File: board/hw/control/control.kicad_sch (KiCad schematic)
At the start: 43 parts, among them IC1 TINY2313, J1 stepper #1, J2 stepper #2, J3 buttons, J4 power, J6 AVR-ISP-10, Q1 MMFTP84W, Q3 2N7002, U1 ULN2003A, U2 ULN2003A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

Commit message: page size adjusted to schematics requirements
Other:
- moved on the sheet: C2, C4, C5, C6, D1, D2, D3, D4, D5, D6, D7, D8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

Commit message: C2 and C4 are not 1206 as they should
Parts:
- C2: footprint Capacitor_SMD:C_0805_2012Metric -> Capacitor_SMD:C_1206_3216Metric_Pad1.33x1.80mm_HandSolder
- C4: footprint Capacitor_SMD:C_0805_2012Metric_Pad1.18x1.45mm_HandSolder -> Capacitor_SMD:C_1206_3216Metric_Pad1.33x1.80mm_HandSolder
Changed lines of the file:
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@@
       (effects (font (size 1.778 1.5113)) (justify left bottom))
     )
-    (property "Footprint" "Capacitor_SMD:C_0805_2012Metric_Pad1.18x1.45mm_HandSolder" (at 116.84 110.49 0)
+    (property "Footprint" "Capacitor_SMD:C_1206_3216Metric_Pad1.33x1.80mm_HandSolder" (at 116.84 110.49 0)
       (effects (font (size 1.27 1.27)) hide)
     )
@@
       (effects (font (size 1.778 1.5113)) (justify left bottom))
     )
-    (property "Footprint" "Capacitor_SMD:C_0805_2012Metric" (at 144.78 72.39 0)
-      (effects (font (size 1.27 1.27)) hide)
-    )
+    (property "Footprint" "Capacitor_SMD:C_1206_3216Metric_Pad1.33x1.80mm_HandSolder" (at 144.78 72.39 0)
+      (effects (font (size 1.27 1.27)) hide)
+    )

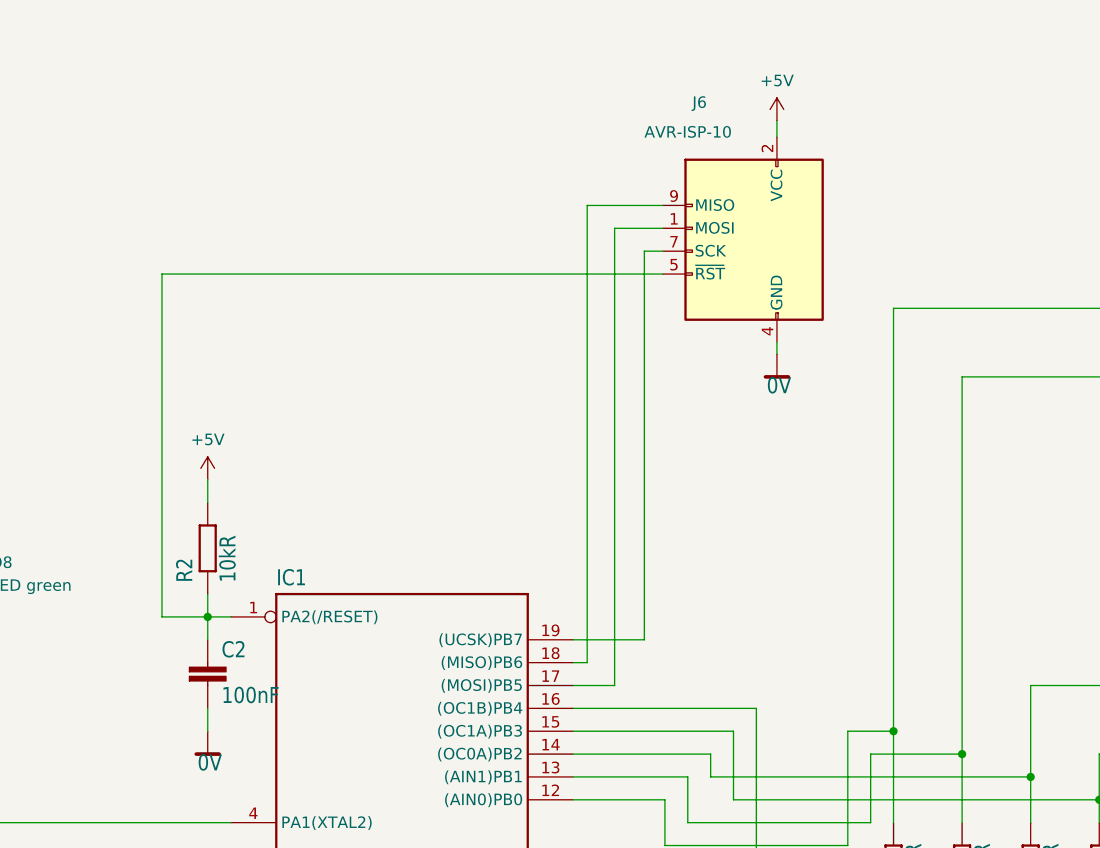
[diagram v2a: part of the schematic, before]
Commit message: added diade so that AVR's ISP can optionaly power the board, but board power will not damage the programmer
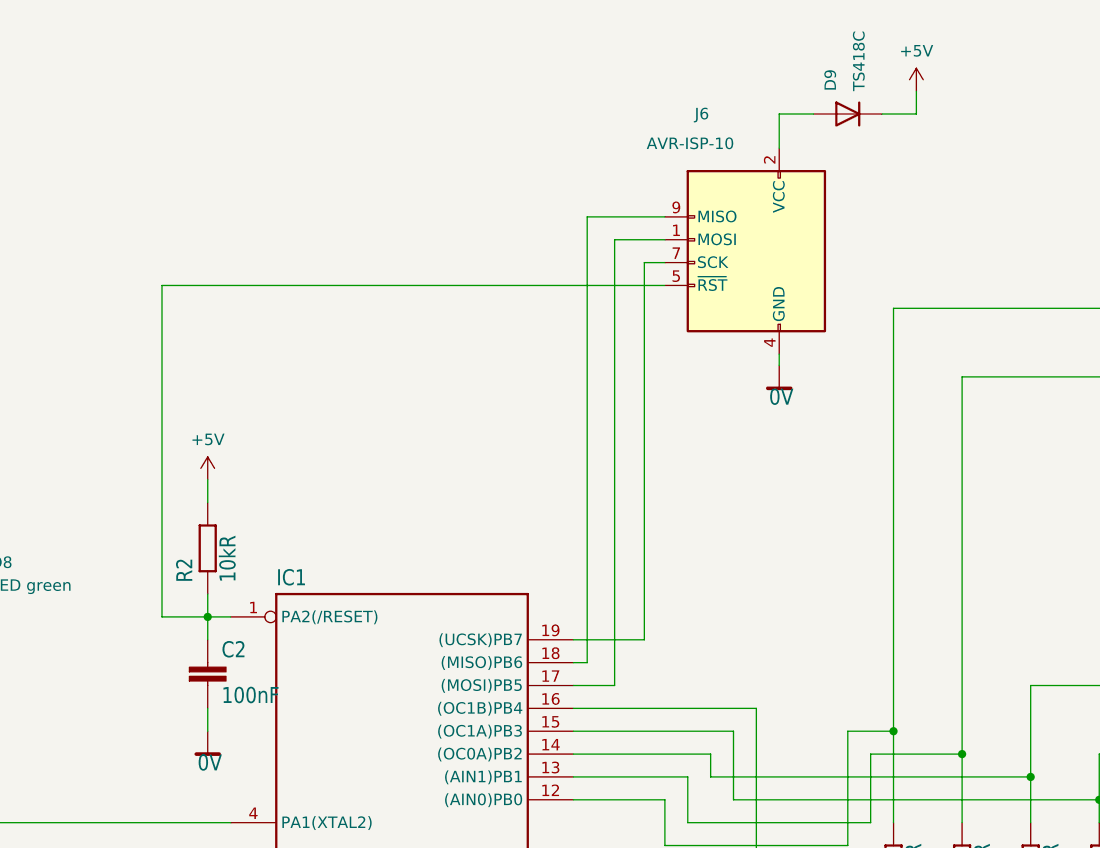
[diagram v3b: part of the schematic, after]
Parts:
- added D9: TS418C, Diode_SMD:D_0805_2012Metric, symbol Diode:CD4148W
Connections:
- net +5V: now also D9.1 (K); no longer J6.2 (VCC)
- new net: D9.2 (A), J6.2 (VCC)
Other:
- moved on the sheet: J6
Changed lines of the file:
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@@
+    (stroke (width 0) (type default))
+  )
+  (wire (pts (xy 223.52 11.43) (xy 223.52 8.89))
     (stroke (width 0) (type default))
   )
@@
     (stroke (width 0) (type default))
   )
+  (wire (pts (xy 208.28 11.43) (xy 212.09 11.43))
+    (stroke (width 0) (type default))
+  )
   (wire (pts (xy 318.135 53.975) (xy 313.69 53.975))
     (stroke (width 0) (type default))
@@
     (stroke (width 0) (type default))
   )
-  (wire (pts (xy 193.294 26.67) (xy 193.294 69.85))
+  (wire (pts (xy 193.294 27.94) (xy 193.294 69.85))
     (stroke (width 0) (type default))
   )
@@
     (stroke (width 0) (type default))
   )
-  (wire (pts (xy 208.026 12.192) (xy 208.026 13.97))
-    (stroke (width 0) (type default))
-  )
   (wire (pts (xy 298.45 135.89) (xy 303.53 135.89))
     (stroke (width 0) (type default))
@@
     (stroke (width 0) (type default))
   )
-  (wire (pts (xy 195.326 21.59) (xy 186.944 21.59))
+  (wire (pts (xy 195.58 22.86) (xy 186.944 22.86))
     (stroke (width 0) (type default))
   )
@@
     (stroke (width 0) (type default))
   )
-  (wire (pts (xy 139.7 29.21) (xy 139.7 67.31))
+  (wire (pts (xy 139.7 30.48) (xy 139.7 67.31))
     (stroke (width 0) (type default))
   )
@@
     (stroke (width 0) (type default))
   )
+  (wire (pts (xy 208.28 39.37) (xy 208.28 38.1))
+    (stroke (width 0) (type default))
+  )
   (wire (pts (xy 271.78 133.35) (xy 271.78 135.89))
     (stroke (width 0) (type default))
@@
     (stroke (width 0) (type default))
   )
-  (wire (pts (xy 189.992 24.13) (xy 189.992 74.93))
+  (wire (pts (xy 189.992 25.4) (xy 189.992 74.93))
     (stroke (width 0) (type default))
   )
@@
     (stroke (width 0) (type default))
   )
-  (wire (pts (xy 139.7 29.21) (xy 195.326 29.21))
+  (wire (pts (xy 139.7 30.48) (xy 195.58 30.48))
     (stroke (width 0) (type default))
   )
@@
     (stroke (width 0) (type default))
   )
-  (wire (pts (xy 186.944 21.59) (xy 186.944 72.39))
+  (wire (pts (xy 186.944 22.86) (xy 186.944 72.39))
     (stroke (width 0) (type default))
   )
@@
     (stroke (width 0) (type default))
   )
-  (wire (pts (xy 195.326 26.67) (xy 193.294 26.67))
-    (stroke (width 0) (type default))
-  )
-  (wire (pts (xy 195.326 24.13) (xy 189.992 24.13))
+  (wire (pts (xy 195.58 27.94) (xy 193.294 27.94))
+    (stroke (width 0) (type default))
+  )
+  (wire (pts (xy 195.58 25.4) (xy 189.992 25.4))
     (stroke (width 0) (type default))
   )
@@
     (stroke (width 0) (type default))
   )
+  (wire (pts (xy 208.28 15.24) (xy 208.28 11.43))
+    (stroke (width 0) (type default))
+  )
   (wire (pts (xy 271.78 173.99) (xy 271.78 176.53))
     (stroke (width 0) (type default))
@@
     (stroke (width 0) (type default))
   )
-  (wire (pts (xy 208.026 36.83) (xy 208.026 38.1))
-    (stroke (width 0) (type default))
-  )
   (wire (pts (xy 97.155 156.21) (xy 120.65 156.21))
     (stroke (width 0) (type default))
@@
   )
   (wire (pts (xy 288.29 95.25) (xy 288.29 96.52))
+    (stroke (width 0) (type default))
+  )
+  (wire (pts (xy 219.71 11.43) (xy 223.52 11.43))
     (stroke (width 0) (type default))
   )
@@
     )
   )
-  (symbol (lib_id "Connector:AVR-ISP-10") (at 205.486 26.67 0) (mirror y) (unit 1)
-    (in_bom yes) (on_board yes) (dnp no)
-    (property "Reference" "J6" (at 198.628 10.16 0)
+  (symbol (lib_id "Connector:AVR-ISP-10") (at 205.74 27.94 0) (mirror y) (unit 1)
+    (in_bom yes) (on_board yes) (dnp no)
+    (property "Reference" "J6" (at 198.882 11.43 0)
       (effects (font (size 1.27 1.27)) (justify right))
     )
-    (property "Value" "AVR-ISP-10" (at 193.294 13.462 0)
+    (property "Value" "AVR-ISP-10" (at 193.548 14.732 0)
       (effects (font (size 1.27 1.27)) (justify right))
     )
-    (property "Footprint" "Connector_IDC:IDC-Header_2x05_P2.54mm_Vertical" (at 211.836 25.4 90)
-      (effects (font (size 1.27 1.27)) hide)
-    )
-    (property "Datasheet" " ~" (at 237.871 40.64 0)
+    (property "Footprint" "Connector_IDC:IDC-Header_2x05_P2.54mm_Vertical" (at 212.09 26.67 90)
+      (effects (font (size 1.27 1.27)) hide)
+    )
+    (property "Datasheet" " ~" (at 238.125 41.91 0)
       (effects (font (size 1.27 1.27)) hide)
     )
@@
     )
   )
-  (symbol (lib_id "control-eagle-import:0V") (at 208.026 40.64 0) (unit 1)
-    (in_bom yes) (on_board yes) (dnp no)
-    (property "Reference" "#SUPPLY015" (at 208.026 40.64 0)
-      (effects (font (size 1.27 1.27)) hide)
-    )
-    (property "Value" "0V" (at 206.883 42.672 0)
-      (effects (font (size 1.778 1.5113)) (justify left bottom))
-    )
-    (property "Footprint" "control:" (at 208.026 40.64 0)
-      (effects (font (size 1.27 1.27)) hide)
-    )
-    (property "Datasheet" "" (at 208.026 40.64 0)
+  (symbol (lib_id "control-eagle-import:0V") (at 208.28 41.91 0) (unit 1)
+    (in_bom yes) (on_board yes) (dnp no)
+    (property "Reference" "#SUPPLY015" (at 208.28 41.91 0)
+      (effects (font (size 1.27 1.27)) hide)
+    )
+    (property "Value" "0V" (at 207.137 43.942 0)
+      (effects (font (size 1.778 1.5113)) (justify left bottom))
+    )
+    (property "Footprint" "control:" (at 208.28 41.91 0)
+      (effects (font (size 1.27 1.27)) hide)
+    )
+    (property "Datasheet" "" (at 208.28 41.91 0)
       (effects (font (size 1.27 1.27)) hide)
     )
@@
         (path "/99b3aba4-a2cc-4425-a477-43f3a410d922"
           (reference "#SUPPLY012") (unit 1)
+        )
+      )
+    )
+  )
+  (symbol (lib_id "Diode:CD4148W") (at 215.9 11.43 0) (mirror y) (unit 1)
+    (in_bom yes) (on_board yes) (dnp no)
+    (property "Reference" "D9" (at 213.995 8.89 90)
+      (effects (font (size 1.27 1.27)) (justify left))
+    )
+    (property "Value" "TS418C" (at 217.17 8.89 90)
+      (effects (font (size 1.27 1.27)) (justify left))
+    )
+    (property "Footprint" "Diode_SMD:D_0805_2012Metric" (at 215.9 16.51 0)
+      (effects (font (size 1.27 1.27)) hide)
+    )
+    (property "Datasheet" "https://www.dccomponents.com/upload/product/original/623524775088.pdf" (at 215.9 11.43 0)
+      (effects (font (size 1.27 1.27)) hide)
+    )
+    (property "Sim.Device" "D" (at 215.9 11.43 0)
+      (effects (font (size 1.27 1.27)) hide)
+    )
+    (property "Sim.Pins" "1=K 2=A" (at 215.9 11.43 0)
+      (effects (font (size 1.27 1.27)) hide)
+    )
+    (pin "1")
+    (pin "2")
+    (instances
+      (project "control"
+        (path "/99b3aba4-a2cc-4425-a477-43f3a410d922"
+          (reference "D9") (unit 1)
         )
       )
@@
     )
   )
-  (symbol (lib_id "power:+5V") (at 208.026 12.192 0) (unit 1)
+  (symbol (lib_id "power:+5V") (at 223.52 8.89 0) (unit 1)
     (in_bom yes) (on_board yes) (dnp no) (fields_autoplaced)
-    (property "Reference" "#PWR013" (at 208.026 16.002 0)
-      (effects (font (size 1.27 1.27)) hide)
-    )
-    (property "Value" "+5V" (at 208.026 7.747 0)
+    (property "Reference" "#PWR013" (at 223.52 12.7 0)
+      (effects (font (size 1.27 1.27)) hide)
+    )
+    (property "Value" "+5V" (at 223.52 4.445 0)
       (effects (font (size 1.27 1.27)))
     )
-    (property "Footprint" "" (at 208.026 12.192 0)
-      (effects (font (size 1.27 1.27)) hide)
-    )
-    (property "Datasheet" "" (at 208.026 12.192 0)
-      (effects (font (size 1.27 1.27)) hide)
-    )
+    (property "Footprint" "" (at 223.52 8.89 0)
+      (effects (font (size 1.27 1.27)) hide)
+    )
+    (property "Datasheet" "" (at 223.52 8.89 0)
+      (effects (font (size 1.27 1.27)) hide)
+    )
